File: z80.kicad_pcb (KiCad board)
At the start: 2 copper layers, 55 parts, among them J201 Conn_02x06_Row_Letter_First, P101 CONN_01X04, P102 CONN_02X20, P103 CONN_01X10, P104 CONN_01X10, P201 Interrupt Daisy Chain SIO, P202 Interrupt Daisy Chain CTC, P203 CONN_02X10, P204 Outputs, P205 Inputs, U101 7400, U102 Z8400, U103 AT28C64B, U104 AS6C1008, U105 74LS138, U106 Z8420, U201 Z8430, U202 Z8440, Y101 4MHz

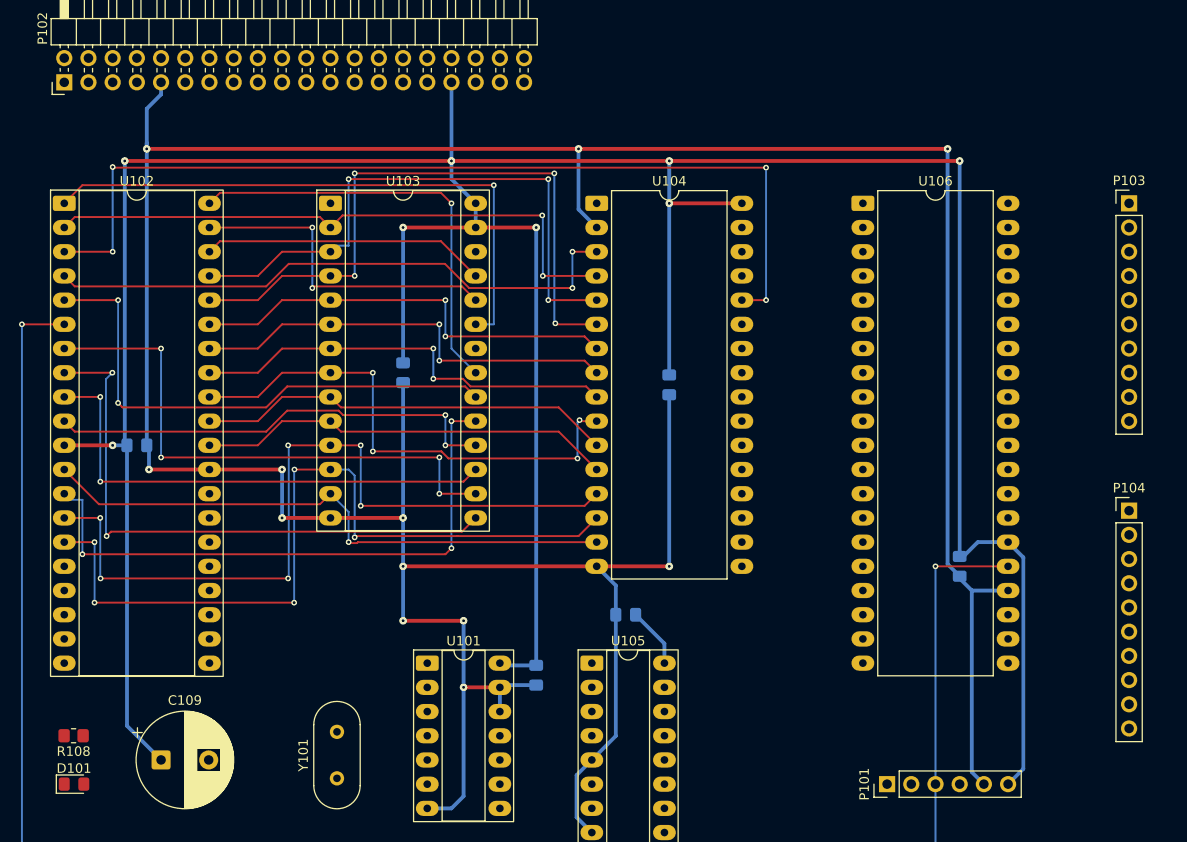
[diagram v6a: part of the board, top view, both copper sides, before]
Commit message: More PCB routing. All ICs on CPU board now routed.
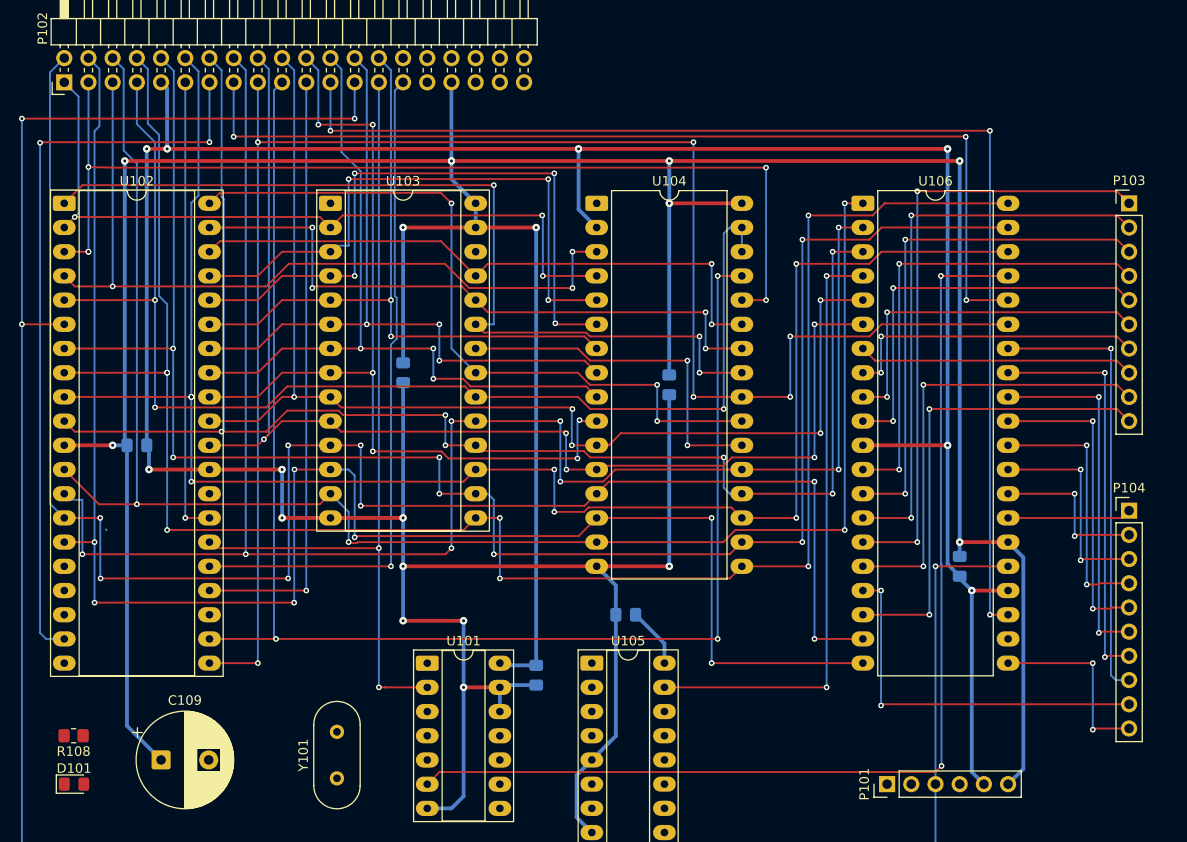
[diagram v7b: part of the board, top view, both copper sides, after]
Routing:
- net ~{RD}: track 0.00 -> 178.5 mm, vias 0 -> 6
- net ~{WR}: track 0.00 -> 152.8 mm, vias 0 -> 3
- net D3: track 62.0 -> 194.8 mm, vias 2 -> 7
- net ~{INT}: track 0.00 -> 127.0 mm, vias 0 -> 3
- net D4: track 58.4 -> 184.1 mm, vias 4 -> 7
- net D7: track 62.8 -> 188.3 mm, vias 3 -> 8
- net D5: track 52.6 -> 177.2 mm, vias 2 -> 7
- net ~{MREQ}: track 0.00 -> 115.7 mm, vias 0 -> 4
- net /~{PIO_M1}: track 0.00 -> 113.3 mm, vias 0 -> 2
- net D2: track 61.9 -> 172.5 mm, vias 1 -> 4
- net D6: track 47.9 -> 157.8 mm, vias 2 -> 6
- net ~{IORQ}: track 0.00 -> 104.1 mm, vias 0 -> 3
- net D1: track 83.8 -> 178.4 mm, vias 5 -> 7
- net D0: track 83.1 -> 177.6 mm, vias 6 -> 8
- net ~{RESET}: track 0.00 -> 86.6 mm, vias 0 -> 2
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
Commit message: Continued layout of timer/sio board
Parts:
- added C202: 0.1u, Capacitor_SMD:C_0805_2012Metric_Pad1.18x1.45mm_HandSolder, F.Cu at (252.7, 188.6)
- added C203: 10u, Capacitor_THT:CP_Radial_D10.0mm_P5.00mm, F.Cu at (226.2, 212.1)
- added D201: LED, LED_SMD:LED_0805_2012Metric_Pad1.15x1.40mm_HandSolder, F.Cu at (219.1, 214.6)
- added P105: CONN_02X20, Connector_PinHeader_2.54mm:PinHeader_2x20_P2.54mm_Horizontal, F.Cu at (212.1, 154.9)
- added R203: 470, Resistor_SMD:R_0805_2012Metric_Pad1.20x1.40mm_HandSolder, F.Cu at (219.1, 210.2)
- C107, C108, R101, R102, R103, R104, R105, R106: moved to B.Cu
- C201: value 10u -> 0.1u; footprint Capacitor_THT:CP_Radial_D10.0mm_P5.00mm -> Capacitor_SMD:C_0805_2012Metric_Pad1.18x1.45mm_HandSolder
- U104: footprint Package_DIP:DIP-32_W15.24mm_LongPads -> Package_DIP:DIP-32_W15.24mm_Socket_LongPads
- moved 10k210 240.4 mm to (297.2, 227.9)
- moved 10k201 234.0 mm to (287.7, 214.7)
- moved 10k202 234.0 mm to (287.7, 217.6)
- moved 10k203 234.0 mm to (287.7, 220.6)
- moved 10k204 234.0 mm to (287.7, 223.5)
- moved 10k209 234.0 mm to (292.4, 220.6)
- moved 10k206 233.4 mm to (287.7, 228.6)
- moved 10k207 229.1 mm to (275.0, 225.0)
- moved 10k208 229.1 mm to (275.0, 228.0)
- moved J201 225.3 mm to (218.4, 231.1), turned to 90 degrees
- moved P203 223.8 mm to (276.2, 193.0)
- moved 10k211 217.2 mm to (287.0, 207.2)
- moved 10k212 217.2 mm to (287.0, 210.2)
- moved 10k215 214.8 mm to (287.0, 203.2)
- moved 10k214 214.2 mm to (287.0, 199.4)
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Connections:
- net Net-(P205-Pin_1) renamed /Timer/CLK/TRG0
- net Net-(P205-Pin_2) renamed /Timer/CLK/TRG1
- net Net-(P205-Pin_3) renamed /Timer/CLK/TRG2
- net Net-(P205-Pin_4) renamed /Timer/CLK/TRG3
- P101 pad 1: ~{RESET} -> /CLK_INT
- P101 pad 2: /CLK_INT -> CLK
- P101 pad 3: CLK -> /CLK_EXT
- P101 pad 4: /CLK_EXT -> ~{RESET}
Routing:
- net CLK: track 252.1 -> 100.7 mm, vias 6 -> 4
- net A5: track 72.0 -> 188.4 mm, vias 2 -> 4
- net A7: track 61.7 -> 160.2 mm, vias 3 -> 6
- net ~{CTC_CE}: track 0.00 -> 85.9 mm, vias 0 -> 2
- net ~{SIO_CE}: track 0.00 -> 83.2 mm, vias 0 -> 1
- net ~{CE_3}: track 0.00 -> 79.5 mm, vias 0 -> 1
- net ~{BUSACK}: track 0.00 -> 78.7 mm, vias 0 -> 1
- net /CLK_INT: track 0.00 -> 78.2 mm, vias 0 -> 1
- net VCC: track 363.1 -> 432.9 mm, vias 9 -> 13
- net ~{RESET}: track 86.6 -> 154.5 mm, vias 2 -> 3
- net GND: track 388.3 -> 438.1 mm
- net ~{M1}: track 48.3 -> 86.1 mm, vias 1 -> 2
- net A4: track 74.5 -> 111.7 mm, vias 3 -> 5
- net A10: track 77.4 -> 113.3 mm, vias 3 -> 4
- net A11: track 94.7 -> 128.6 mm, vias 3 -> 4
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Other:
- board text added: "CLK"
- board text added: "CLK/TRG0"
- board text added: "CLK/TRG1"
- board text added: "CLK/TRG2"
- board text added: "CLK/TRG3"
- board text added: "EXT CLK"
- board text added: "GND"
- board text added: "INT CLK"
- board text added: "VCC"
- board text added: "ZC/TO0"
- board text added: "ZC/TO1"
- board text added: "ZC/TO2"
- board text added: "~{RESET}"
